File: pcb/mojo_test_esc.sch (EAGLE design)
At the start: 12 parts

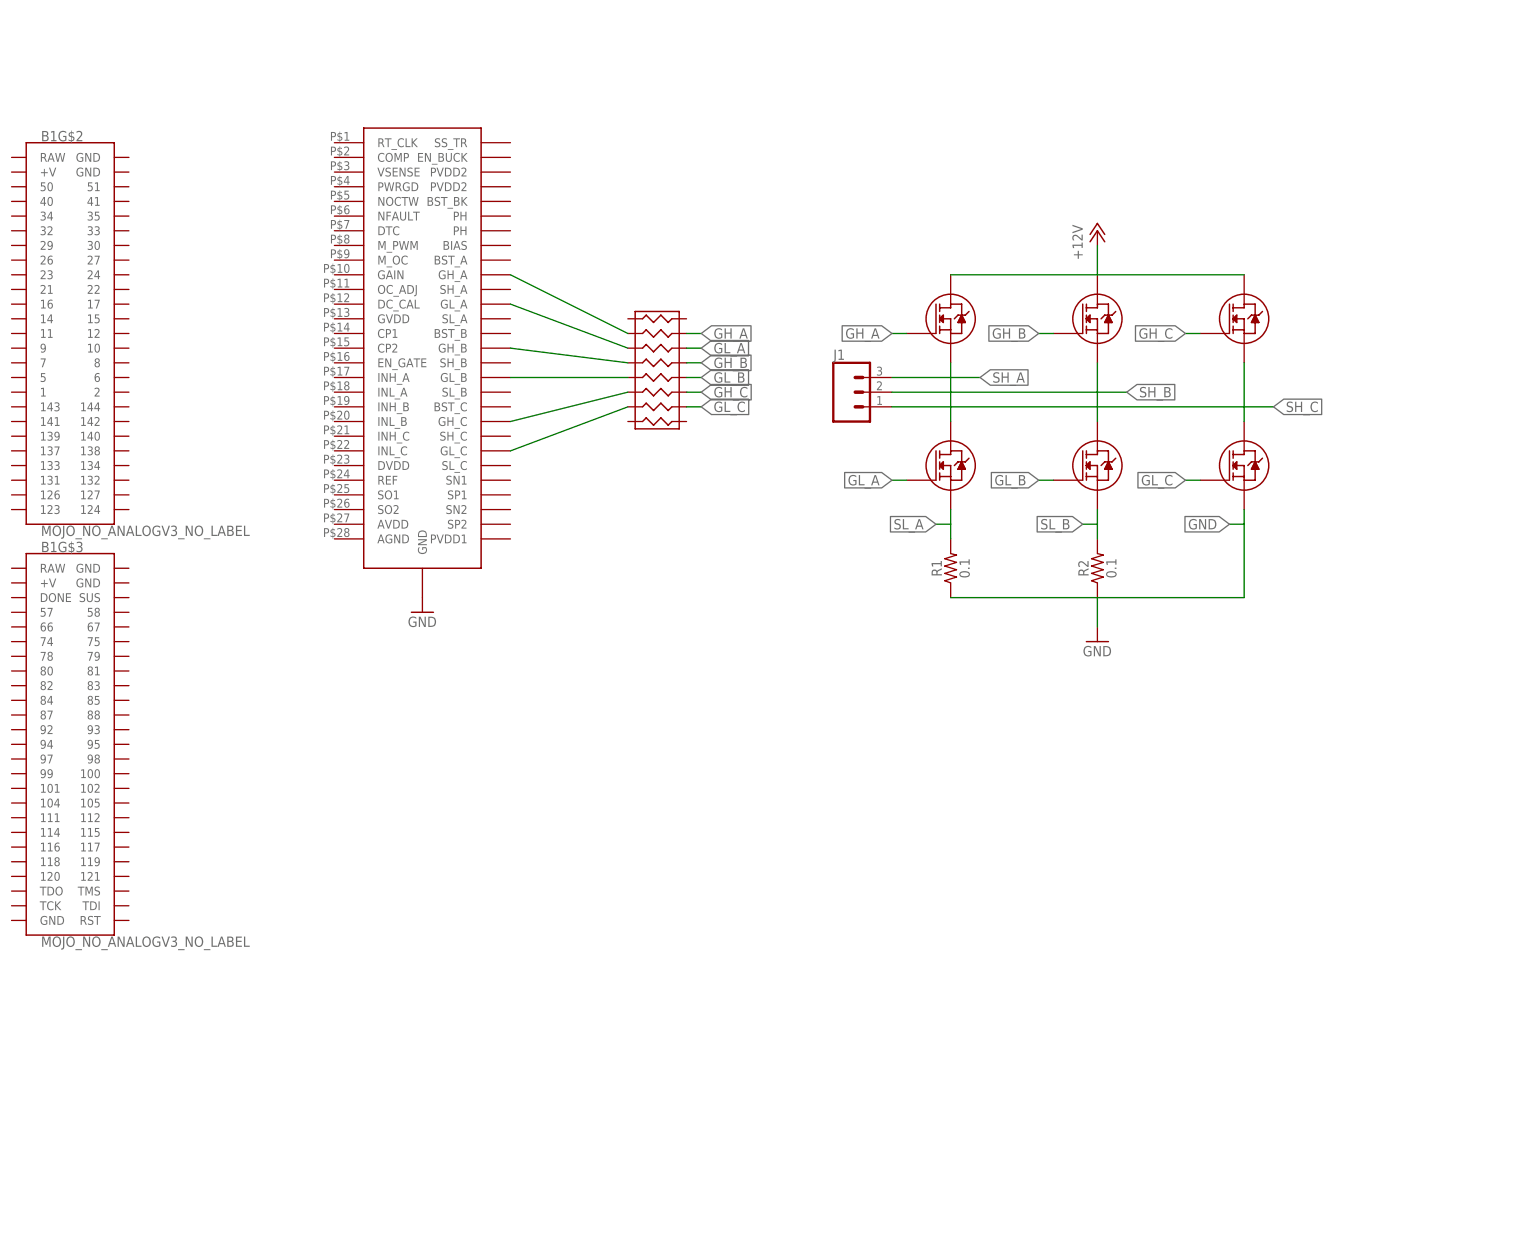
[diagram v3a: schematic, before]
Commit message: Initial layout with capacitors
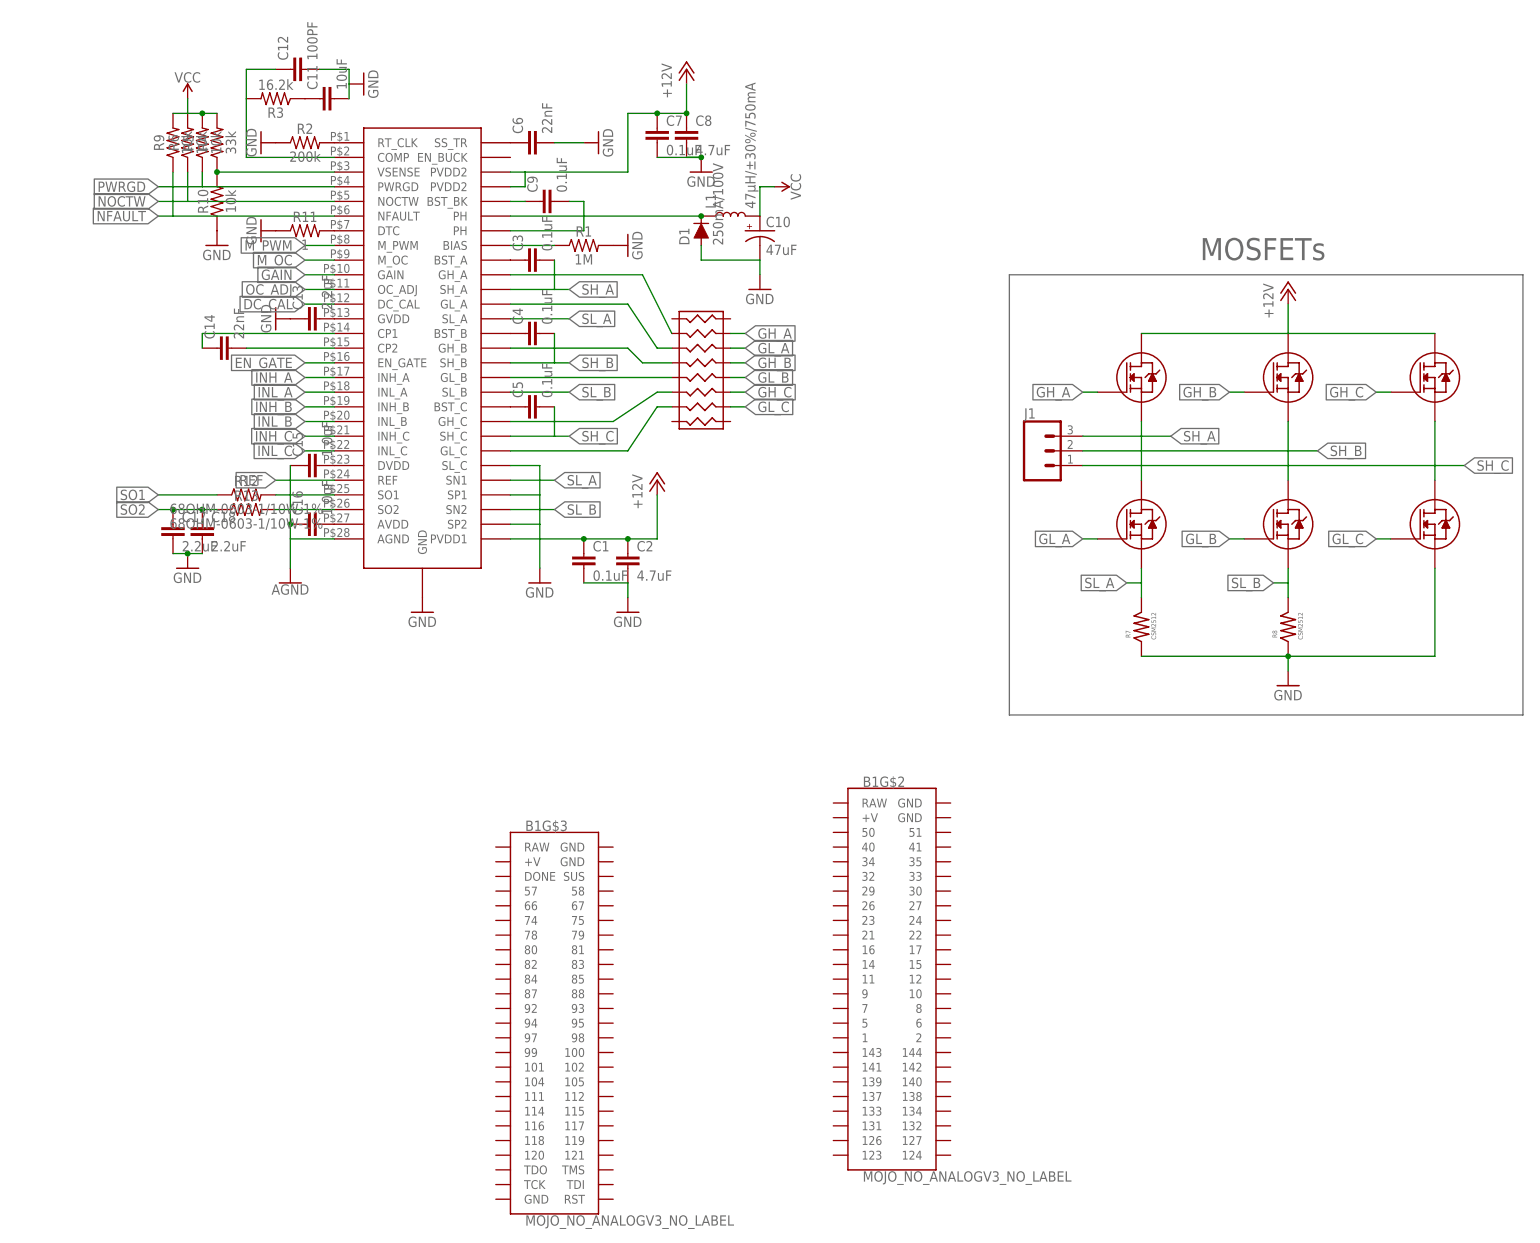
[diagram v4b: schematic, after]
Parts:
- added C1, C3, C4, C5, C7, C9: 0.1uF, SparkFun-Capacitors:0.1UF-0402-16V-10%
- added C10: 47uF, SparkFun-Capacitors:47UF-POLAR-EIA3528-10V-10%
- added C11: 10uF, SparkFun-Capacitors:10UF-0603-6.3V-20%
- added C12: 100PF, SparkFun-Capacitors:100PF-0402-50V-5%
- added C13, C17, C18: 2.2uF, SparkFun-Capacitors:2.2UF-0603-10V-20%
- added C14, C6: 22nF, SparkFun-Capacitors:22NF/22,000PF-0603-50V-10%
- added C15, C16: 1.0uF, SparkFun-Capacitors:1.0UF-0402-16V-10%
- added C2, C8: 4.7uF, SparkFun-Capacitors:4.7UF0603
- added D1: 250mA/100V, SparkFun-DiscreteSemi:DIODE-BAS16J
- added L1: 47µH/±30%/750mA, SparkFun-Coils:INDUCTOR-CR54-47UH
- added R10, R5, R6, R9: 10k, SparkFun-Resistors:10KOHM-0603-1/10W-1%
- added R11: 1, SparkFun-Resistors:1OHM-0603-1/10W-1%
- added R12, R13: 68OHM-0603-1/10W-1%, SparkFun-Resistors:68OHM-0603-1/10W-1%
- added R3: 16.2k, SparkFun-Resistors:16.2KOHM-0603-1/10W-1%
- added R4: 33k, SparkFun-Resistors:33KOHM-0603-1/10W-1%
- added R7, R8: CSM2512, mojo_test_esc:CSM2512
- R1: value 0.1 -> 1M; device SparkFun-Resistors:0.1OHM-1210-1/2W-1% -> SparkFun-Resistors:1MOHM-0603-1/4W-5%
- R2: value 0.1 -> 200k; device SparkFun-Resistors:0.1OHM-1210-1/2W-1% -> SparkFun-Resistors:200KOHM-0603-1/10W-1%
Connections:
- new net AGND: C15.1, C16.1, U$1.AGND
- new net DC_CAL: U$1.DC_CAL
- new net EN_GATE: U$1.EN_GATE
- new net GAIN: U$1.GAIN
- new net GL_A_BEF_RES: U$1.GL_A, U$2.P3B
- new net INH_A: U$1.INH_A
- new net INH_B: U$1.INH_B
- new net INH_C: U$1.INH_C
- new net INL_A: U$1.INL_A
- new net INL_B: U$1.INL_B
- new net INL_C: U$1.INL_C
- new net M_OC: U$1.M_OC
- new net M_PWM: U$1.M_PWM
- new net N$10: C9.1, U$1.BST_BK
- new net N$11: C9.2, D1.C, L1.1, U$1.PH@1, U$1.PH@2
- new net N$12: R2.2, U$1.RT_CLK
- new net N$13: R1.1, U$1.BIAS
- new net N$14: C12.1, R3.2, U$1.COMP
- new net N$15: C11.1, R3.1
- new net N$16: R11.2, U$1.DTC
- new net N$17: C13.2, U$1.GVDD
- new net N$18: C14.1, U$1.CP1
- new net N$19: R10.2, R4.1, U$1.VSENSE
- new net N$20: C14.2, U$1.CP2
- new net N$21: C15.2, U$1.DVDD
- new net N$22: C16.2, U$1.AVDD
- new net N$23: R12.2, U$1.SO1
- new net N$24: R13.2, U$1.SO2
- new net N$7: C3.1, U$1.BST_A
- new net N$8: C4.1, U$1.BST_B
- new net N$9: C5.1, U$1.BST_C
- new net NFAULT: R9.1, U$1.NFAULT
- new net NOCTW: R6.1, U$1.NOCTW
- new net OC_ADJ: U$1.OC_ADJ
- new net PWRGD: R5.1, U$1.PWRGD
- new net REF: U$1.REF
- new net SO1: R12.1
- new net SO2: C17.1, C18.1, R13.1
- new net VCC: C10.+, L1.2, R4.2, R5.2, R6.2, R9.2
- net +12V: now also C1.1, C2.1, C7.1, C8.1, U$1.PVDD1, U$1.PVDD2@1, U$1.PVDD2@2
- net GH_A: no longer U$2.P2B
- net GH_B: no longer U$2.P4B
- net GH_C: no longer U$2.P6B
- net GL_A: no longer U$2.P3B
- net GL_B: no longer U$2.P5B
- net GL_C: no longer U$2.P7B
- net GND: now also C1.2, C10.-, C11.2, C12.2, C13.1, C17.2, C18.2, C2.2, C6.2, C7.2, C8.2, D1.A, R1.2, R10.1, R11.1, R7.P$1, R8.P$1, U$1.SL_C, U$1.SP1, U$1.SP2; no longer R1.1
- net N$1: now also U$2.P2B; no longer U$2.P2
- net N$2: now also C6.1, U$1.SS_TR; no longer U$1.GL_A, U$2.P3
- net N$3: now also U$2.P4B; no longer U$2.P4
- net N$4: now also U$2.P5B; no longer U$2.P5
- net N$5: now also U$2.P6B; no longer U$2.P6
- net N$6: now also U$2.P7B; no longer U$2.P7
- net SH_A: now also C3.2, U$1.SH_A
- net SH_B: now also C4.2, U$1.SH_B
- net SH_C: now also C5.2, U$1.SH_C
- net SL_A: now also R7.P$2, U$1.SL_A, U$1.SN1; no longer R1.2
- net SL_B: now also R8.P$2, U$1.SL_B, U$1.SN2; no longer R2.2
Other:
- note added: "MOSFETs"
- moved on the sheet: B1G$2, B1G$3, J1, R1, R2
